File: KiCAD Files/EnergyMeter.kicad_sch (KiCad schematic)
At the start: 7 parts, among them J1 Screw_Terminal_AC

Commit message: update
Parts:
- F1: value 1A/250VAC, SLOW, socketed -> 500mA, SLOW, socketed
- J1: LCSC Part # C409161 -> C707824
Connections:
- net AC-OUT1: now reaches FL1.2, PS1.1 (AC/L)
- net AC-OUT2: now reaches FL1.4, PS1.2 (AC/N)
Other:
- moved on the sheet: C2, J1, PS1

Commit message: Schematic update
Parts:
- removed PS1: HLK-PM03, Converter_ACDC:Converter_ACDC_Hi-Link_HLK-PMxx, symbol Converter_ACDC:HLK-PM03
- added C10, C3, C5: 10u, symbol Device:C_Small
- added C11, C12, C13: 33n, symbol Device:C_Small
- added C4, C6, C8, C9: 100n, symbol Device:C_Small
- added C7: 100u tant, symbol Device:C_Polarized_Small
- added D1: RED, symbol Device:LED_Small
- added J2: Conn_01x05, symbol Connector_Generic:Conn_01x05
- added PS1: HLK-PM01, Converter_ACDC:Converter_ACDC_Hi-Link_HLK-PMxx, symbol Converter_ACDC:HLK-PM01
- added R1: 330R, symbol Device:R_Small
- added R10, R11, R12: 1k, symbol Device:R_Small
- added R13, R14, R15, R16: 470k, symbol Device:R_Small
- added R2, R3, R4, R5: 10k, symbol Device:R_Small
- added R6, R7, R8, R9: 0.004R, symbol Device:R
- added SW1: SW_Push, symbol Switch:SW_Push
- added U1: AMS1117-3.3, Package_TO_SOT_SMD:SOT-223-3_TabPin2, symbol Regulator_Linear:AMS1117-3.3
- added U2: ESP-12F, RF_Module:ESP-12E, symbol RF_Module:ESP-12F
- added U3: HLW8032, symbol Symbol_Library:HLW8032
- C2: value MAL203851101E3 -> 100u
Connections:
- net N: now reaches C1.2, FL1.3, J1.1 (Pin_1), RV1.2
- net N: now also R11.1, R6.2, R7.2, R8.2, R9.2
- net L: now reaches F1.1, J1.2 (Pin_2)
- net L: now also R10.1, R13.1, R6.1, R7.1, R8.1, R9.1
- net GND: now reaches C2.2
- net GND: now also C10.2, C11.2, C12.2, C13.2, C3.2, C4.2, C5.2, C6.2, C7.2, C8.2, C9.2, D1.1 (K), J2.5 (Pin_5), PS1.3 (-Vout), R12.1, R2.2, SW1.2, U1.1 (GND), U2.15 (GND), U3.5 (GND)
- net +5V: now reaches C2.1
- net +5V: now also C10.1, C3.1, C4.1, C9.1, PS1.4 (+Vout), U1.3 (VI), U3.1 (VDD)
- net AC-OUT1: no longer names the net of FL1.2
- net AC-OUT1: now also PS1.1 (AC/L)
- net AC-OUT2: no longer names the net of FL1.4
- net AC-OUT2: now also PS1.2 (AC/N)
- new net: D1.2 (A), R1.2
- new net: R14.2, R15.1
- new net: R15.2, R16.1
- new net: C13.1, R12.2, R16.2, U3.4 (VP)
- new net: C12.1, R11.2, U3.3 (IN)
- new net: C11.1, R10.2, U3.2 (IP)
- new net: R2.1, U2.16 (GPIO15)
- new net: R5.2, U2.3 (EN)
- new net: R13.2, R14.1
- new net +3.3V: C5.1, C6.1, C7.1, C8.1, R1.1, R3.1, R4.1, R5.1, U1.2 (VO), U2.8 (VCC)
- new net DTR: J2.3 (Pin_3), R4.2, U2.18 (GPIO0)
- new net PF: U2.19 (GPIO4)
- new net RESET: J2.4 (Pin_4), R3.2, SW1.1, U2.1 (~{RST})
- new net RX: J2.1 (Pin_1), U2.22 (GPIO1/TXD)
- new net TX: J2.2 (Pin_2), U2.21 (GPIO3/RXD)
- no-connect marks 0 -> 13
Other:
- note added: "230VAC >> 5VDC"
- note added: "5VDC >> 3.3VDC"
- note added: "MICROCONTROLLER"
- note added: "PROG. PORT"
- note added: "TO-DO: - BOM needs to include both the fuse and fuse socket - all symbols need to contain LCSC part number - add every datasheet link to BOM - logic level conversion (IC to ESP) DONE: - 3.3V voltage regulator for MCU"
- note removed: "TO-DO: - tool-less terminals - BOM needs to include both the fuse and fuse socket - all symbols need to contain LCSC part number - EnergyMeter IC to MCU logic level conversion - 3.3V voltage regulator for MCU - add every datasheet link to BOM"
- moved on the sheet: C1, C2, F1, FL1, J1, RV1

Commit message: Schematic update
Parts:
- added J3: Screw_Terminal_AC, symbol Connector:Screw_Terminal_01x02
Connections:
- net L: no longer R13.1
- net N: now also R13.1, J3.1 (Pin_1); no longer R11.1, R6.2, R7.2, R8.2, R9.2
- new net: J3.2 (Pin_2), R11.1, R6.2, R7.2, R8.2, R9.2
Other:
- moved on the sheet: C10, C11, C12, C13, C9, R10, R11, R12, R13, R14, R15, R16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

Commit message: TO-DO update
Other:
- note added: "TO-DO: - logic level conversion (IC to ESP) - BOM needs to include both the fuse and fuse socket - all symbols need to contain LCSC part number - add every datasheet link to BOM DONE: - 3.3V voltage regulator for MCU"
- note removed: "TO-DO: - BOM needs to include both the fuse and fuse socket - all symbols need to contain LCSC part number - add every datasheet link to BOM - logic level conversion (IC to ESP) DONE: - 3.3V voltage regulator for MCU"
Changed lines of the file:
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@@
 		)
 	)
-	(text "TO-DO:\n\n- BOM needs to include both the fuse and fuse socket\n- all symbols need to contain LCSC part number\n- add every datasheet link to BOM\n- logic level conversion (IC to ESP)\n\nDONE:\n- 3.3V voltage regulator for MCU\n"
+	(text "TO-DO:\n\n- logic level conversion (IC to ESP)\n- BOM needs to include both the fuse and fuse socket\n- all symbols need to contain LCSC part number\n- add every datasheet link to BOM\n\nDONE:\n\n- 3.3V voltage regulator for MCU\n"
 		(exclude_from_sim no)
 		(at 226.822 155.194 0)

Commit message: Schematic update
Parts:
- added JP1: Jumper_2_Bridged, symbol Jumper:Jumper_2_Bridged
- added Q1, Q2: BSS138, Package_TO_SOT_SMD:SOT-23, symbol Transistor_FET:BSS138
- added Q3, Q4: S8050-SOT23, Package_TO_SOT_SMD:SOT-23, symbol Symbol_Library:S8050-SOT23
- added R17, R18, R19, R20, R21, R22: 10k, Resistor_SMD:R_0805_2012Metric, symbol Device:R_Small
- C1: footprint (none) -> Capacitor_THT:C_Rect_L18.0mm_W8.0mm_P15.00mm_FKS3_FKP3; LCSC Part # C105712 -> C93321
- C10, C3, C5: footprint (none) -> Capacitor_SMD:C_1206_3216Metric
- C11, C12, C13, C4, C6, C8, C9: footprint (none) -> Capacitor_SMD:C_0805_2012Metric
- C2: footprint (none) -> Capacitor_THT:CP_Radial_D8.0mm_P3.50mm
- C7: footprint (none) -> Capacitor_Tantalum_SMD:CP_EIA-7343-15_Kemet-W
- D1: footprint (none) -> LED_SMD:LED_0805_2012Metric
- J3: value Screw_Terminal_AC -> Screw_Terminal_LOAD
- R1, R10, R11, R12, R13, R14, R15, R16, R2, R3, R4, R5: footprint (none) -> Resistor_SMD:R_0805_2012Metric
- U3: footprint (none) -> Package_SO:SOP-8_3.9x4.9mm_P1.27mm; LCSC Part # (none) -> C128023; LCSC Part# C128023 -> (none)
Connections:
- net +3.3V: now also Q1.1 (G), Q2.1 (G), R17.1, R19.1
- net +5V: now also R18.1, R20.1
- net DTR: now also Q4.2 (E), R21.2; no longer R4.2, U2.18 (GPIO0)
- net L: now also J3.1 (Pin_1), R13.1; no longer R10.1, R6.1, R7.1, R8.1, R9.1
- net N: now also R10.1, R6.1, R7.1, R8.1, R9.1; no longer J3.1 (Pin_1), R13.1
- net PF: now also Q2.2 (S), R19.2
- net RESET: now also Q3.3 (C); no longer J2.4 (Pin_4)
- net TX: now also JP1.1 (A)
- net HLW8032 TX: now reaches U3.6 (TX)
- net HLW8032 TX: now also Q1.3 (D), R18.2
- net HLW8032 PF: now reaches U3.7 (PF)
- net HLW8032 PF: now also Q2.3 (D), R20.2
- new net: JP1.2 (B), Q1.2 (S), R17.2
- new net: Q3.1 (B), R21.1
- new net: Q4.1 (B), R22.1
- new net GPIO0: Q4.3 (C), R4.2, U2.18 (GPIO0)
- new net RTS: J2.4 (Pin_4), Q3.2 (E), R22.2
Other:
- note added: "ENERGY METER IC"
- note added: "LOGIC LEVEL CONVERSION"
- note added: "PROG. PORT AND AUTO-RESET CIRCUIT"
- note added: "TO-DO: - add footprints - BOM needs to include both the fuse and fuse socket - BOM needs to include jumper - all symbols need to contain LCSC part number - add every datasheet link to BOM - vidjeti što imam od ovih komponenata"
- note removed: "PROG. PORT"
- note removed: "TO-DO: - logic level conversion (IC to ESP) - BOM needs to include both the fuse and fuse socket - all symbols need to contain LCSC part number - add every datasheet link to BOM DONE: - 3.3V voltage regulator for MCU"
- moved on the sheet: C10, C11, C12, C13, C3, C4, C5, C6, C7, C8, C9, D1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

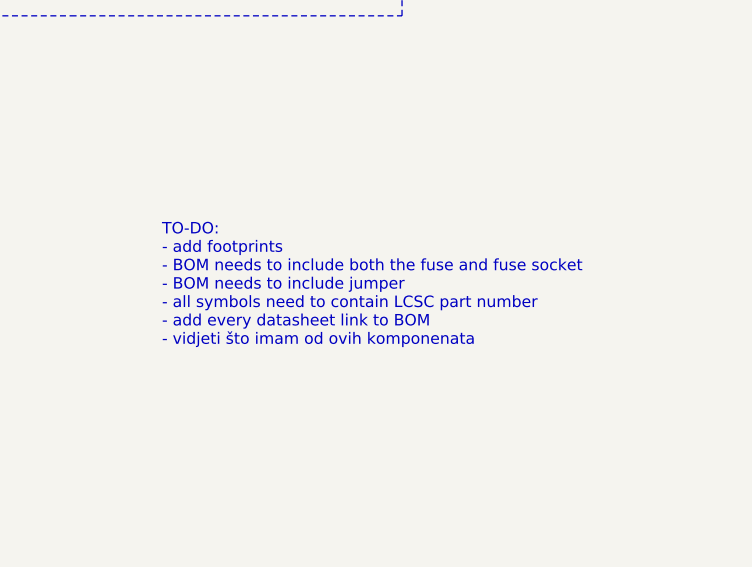
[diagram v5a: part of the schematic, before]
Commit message: schematic update
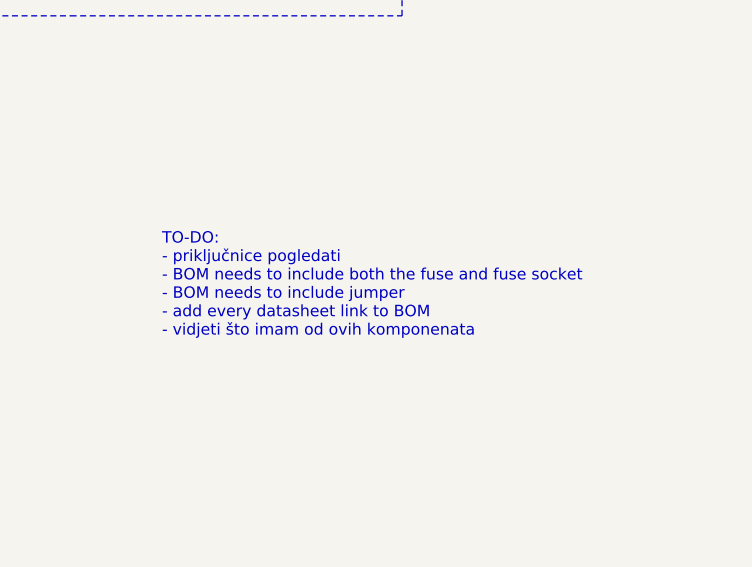
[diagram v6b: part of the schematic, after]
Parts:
- F1: footprint (none) -> Library:FH1-200CK-G
- FL1: footprint (none) -> Library:YDUU9.8-103L0301
- J2: footprint (none) -> Connector_PinHeader_2.54mm:PinHeader_1x05_P2.54mm_Horizontal
- JP1: footprint (none) -> Connector_PinHeader_2.54mm:PinHeader_1x02_P2.54mm_Vertical
- R6, R7, R8, R9: footprint (none) -> Library:R_2512_Shunt
- RV1: footprint (none) -> Varistor:RV_Disc_D12mm_W3.9mm_P7.5mm
- SW1: footprint (none) -> Button_Switch_SMD:SW_Tactile_SPST_NO_Straight_CK_PTS636Sx25SMTRLFS
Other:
- note added: "TO-DO: - priključnice pogledati - BOM needs to include both the fuse and fuse socket - BOM needs to include jumper - add every datasheet link to BOM - vidjeti što imam od ovih komponenata"
- note removed: "TO-DO: - add footprints - BOM needs to include both the fuse and fuse socket - BOM needs to include jumper - all symbols need to contain LCSC part number - add every datasheet link to BOM - vidjeti što imam od ovih komponenata"
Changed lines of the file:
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@@
 		)
 	)
-	(text "TO-DO:\n- add footprints\n- BOM needs to include both the fuse and fuse socket\n- BOM needs to include jumper\n- all symbols need to contain LCSC part number\n- add every datasheet link to BOM\n- vidjeti što imam od ovih komponenata\n"
+	(text "TO-DO:\n- priključnice pogledati\n- BOM needs to include both the fuse and fuse socket\n- BOM needs to include jumper\n- add every datasheet link to BOM\n- vidjeti što imam od ovih komponenata\n"
 		(exclude_from_sim no)
 		(at 227.33 153.162 0)
@@
 			)
 		)
-		(property "Footprint" ""
+		(property "Footprint" "Library:FH1-200CK-G"
 			(at 53.34 26.67 0)
 			(effects
@@
 			)
 		)
-		(property "Footprint" ""
+		(property "Footprint" "Connector_PinHeader_2.54mm:PinHeader_1x02_P2.54mm_Vertical"
 			(at 26.67 153.67 0)
 			(effects
@@
 			)
 		)
-		(property "Footprint" ""
+		(property "Footprint" "Button_Switch_SMD:SW_Tactile_SPST_NO_Straight_CK_PTS636Sx25SMTRLFS"
 			(at 172.72 106.68 0)
 			(effects
@@
 			)
 		)
-		(property "Footprint" ""
+		(property "Footprint" "Library:R_2512_Shunt"
 			(at 49.022 86.36 90)
 			(effects
@@
 			)
 		)
-		(property "Footprint" ""
+		(property "Footprint" "Varistor:RV_Disc_D12mm_W3.9mm_P7.5mm"
 			(at 68.072 33.02 90)
 			(effects
@@
 			)
 		)
-		(property "Footprint" ""
+		(property "Footprint" "Library:R_2512_Shunt"
 			(at 60.452 86.36 90)
 			(effects
@@
 			)
 		)
-		(property "Footprint" ""
+		(property "Footprint" "Library:R_2512_Shunt"
 			(at 37.592 86.36 90)
 			(effects
@@
 			)
 		)
-		(property "Footprint" ""
+		(property "Footprint" "Library:R_2512_Shunt"
 			(at 71.882 86.36 90)
 			(effects
@@
 			)
 		)
-		(property "Footprint" ""
+		(property "Footprint" "Library:YDUU9.8-103L0301"
 			(at 118.11 32.004 0)
 			(effects
@@
 			)
 		)
-		(property "Footprint" ""
+		(property "Footprint" "Connector_PinHeader_2.54mm:PinHeader_1x05_P2.54mm_Horizontal"
 			(at 139.7 149.86 0)
 			(effects

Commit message: Layout
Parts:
- FL1: symbol Device:Filter_EMI_CommonMode -> Symbol_Library:Filter_EMI_EnergyMeter
- J1, J3: footprint (none) -> Library:KF7.62-2P; now in the parts list
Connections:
- net L: now also J3.2 (Pin_2); no longer J3.1 (Pin_1)
- net at R11.1, R6.2, R7.2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: now also J3.1 (Pin_1); no longer J3.2 (Pin_2)
- net at C1.1, F1.2, RV1.1: now also FL1.2; no longer FL1.1
- net at PS1.1 (AC/L): now also FL1.1; no longer FL1.2
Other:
- note added: "TO-DO: - galvanski odvojiti signale - provjeriti pinout od choke - BOM needs to include both the fuse and fuse socket - BOM needs to include jumper - add every datasheet link to BOM - vidjeti što imam od ovih komponenata"
- note removed: "TO-DO: - priključnice pogledati - BOM needs to include both the fuse and fuse socket - BOM needs to include jumper - add every datasheet link to BOM - vidjeti što imam od ovih komponenata"
- moved on the sheet: J3
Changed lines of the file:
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@@
 		)
 	)
-	(text "TO-DO:\n- priključnice pogledati\n- BOM needs to include both the fuse and fuse socket\n- BOM needs to include jumper\n- add every datasheet link to BOM\n- vidjeti što imam od ovih komponenata\n"
+	(text "TO-DO:\n- galvanski odvojiti signale\n- provjeriti pinout od choke\n- BOM needs to include both the fuse and fuse socket\n- BOM needs to include jumper\n- add every datasheet link to BOM\n- vidjeti što imam od ovih komponenata\n"
 		(exclude_from_sim no)
 		(at 227.33 153.162 0)
@@
 		(unit 1)
 		(exclude_from_sim no)
-		(in_bom no)
-		(on_board no)
+		(in_bom yes)
+		(on_board yes)
 		(dnp no)
-		(fields_autoplaced yes)
 		(property "Reference" "J1"
-			(at 25.4 25.4 0)
+			(at 25.654 26.67 0)
 			(effects
 				(font
@@
 		)
 		(property "Value" "Screw_Terminal_AC"
-			(at 25.4 27.94 0)
+			(at 25.4 28.702 0)
 			(effects
 				(font
@@
 			)
 		)
-		(property "Footprint" ""
+		(property "Footprint" "Library:KF7.62-2P"
 			(at 25.4 34.29 0)
 			(effects
@@
 	(symbol
 		(lib_id "Connector:Screw_Terminal_01x02")
-		(at 26.67 95.25 180)
+		(at 26.67 92.71 0)
+		(mirror y)
 		(unit 1)
 		(exclude_from_sim no)
-		(in_bom no)
-		(on_board no)
+		(in_bom yes)
+		(on_board yes)
 		(dnp no)
-		(fields_autoplaced yes)
 		(property "Reference" "J3"
-			(at 26.67 86.36 0)
+			(at 26.416 88.138 0)
 			(effects
 				(font
@@
 		)
 		(property "Value" "Screw_Terminal_LOAD"
-			(at 26.67 88.9 0)
+			(at 26.67 89.916 0)
 			(effects
 				(font
@@
 			)
 		)
-		(property "Footprint" ""
-			(at 26.67 95.25 0)
+		(property "Footprint" "Library:KF7.62-2P"
+			(at 26.67 92.71 0)
 			(effects
 				(font
@@
 		)
 		(property "Datasheet" "~"
-			(at 26.67 95.25 0)
+			(at 26.67 92.71 0)
 			(effects
 				(font
@@
 		)
 		(property "Description" "Generic screw terminal, single row, 01x02, script generated (kicad-library-utils/schlib/autogen/connector/)"
-			(at 26.67 95.25 0)
+			(at 26.67 92.71 0)
 			(effects
 				(font
@@
 		)
 		(property "LCSC Part #" "C707824"
-			(at 26.67 95.25 0)
+			(at 26.67 92.71 0)
 			(effects
 				(font
@@
 	)
 	(symbol
-		(lib_id "Device:Filter_EMI_CommonMode")
+		(lib_id "Symbol_Library:Filter_EMI_EnergyMeter")
 		(at 118.11 33.02 0)
 		(unit 1)

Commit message: pcb layout
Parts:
- added H1, H2, H3, H4: MountingHole, MountingHole:MountingHole_3.2mm_M3, symbol Mechanical:MountingHole
- U3: footprint Package_SO:SOP-8_3.9x4.9mm_P1.27mm -> Library:SOP-8_3.9x4.9mm_P1.27mm_custom
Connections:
- net L: now also J3.1 (Pin_1); no longer J3.2 (Pin_2)
- net at R11.1, R6.2, R7.2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: now also J3.2 (Pin_2); no longer J3.1 (Pin_1)
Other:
- moved on the sheet: J3
